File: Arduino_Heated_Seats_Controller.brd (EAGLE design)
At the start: 40.3 x 35.5 mm, 22 parts, among them U1 MEGA8-AI, U2 UA78M05CDCY, U3 ULN2003ADE4, U4 IC_TD62783-SO-18W

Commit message: Additional silkscreen and trace width tweaks before sending to OSH Park (still v4).
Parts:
- moved R1 0.06 mm to (14.0, 28.6)
- moved R2 0.06 mm to (16.6, 28.6)
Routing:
- net D3: track 24.0 -> 41.4 mm

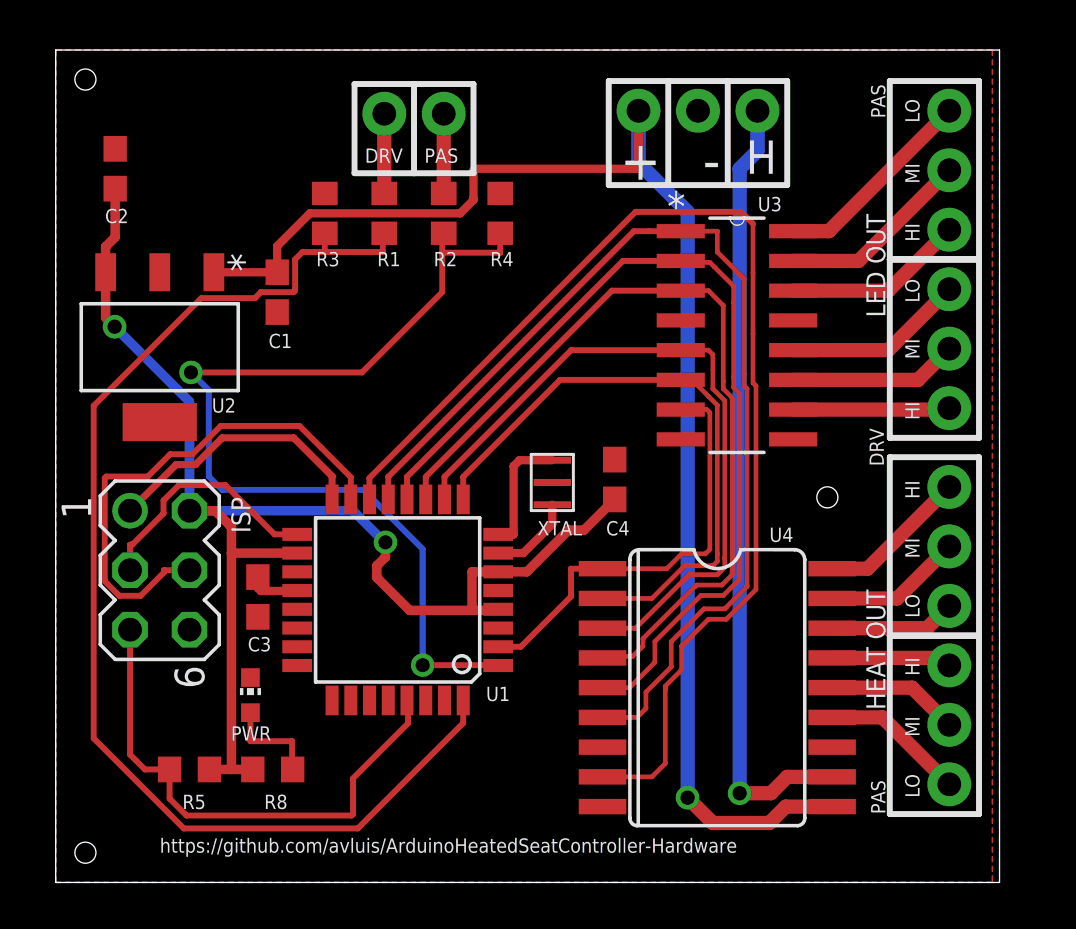
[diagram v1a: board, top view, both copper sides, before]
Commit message: Small position tweak to allow ground pour around connectors.
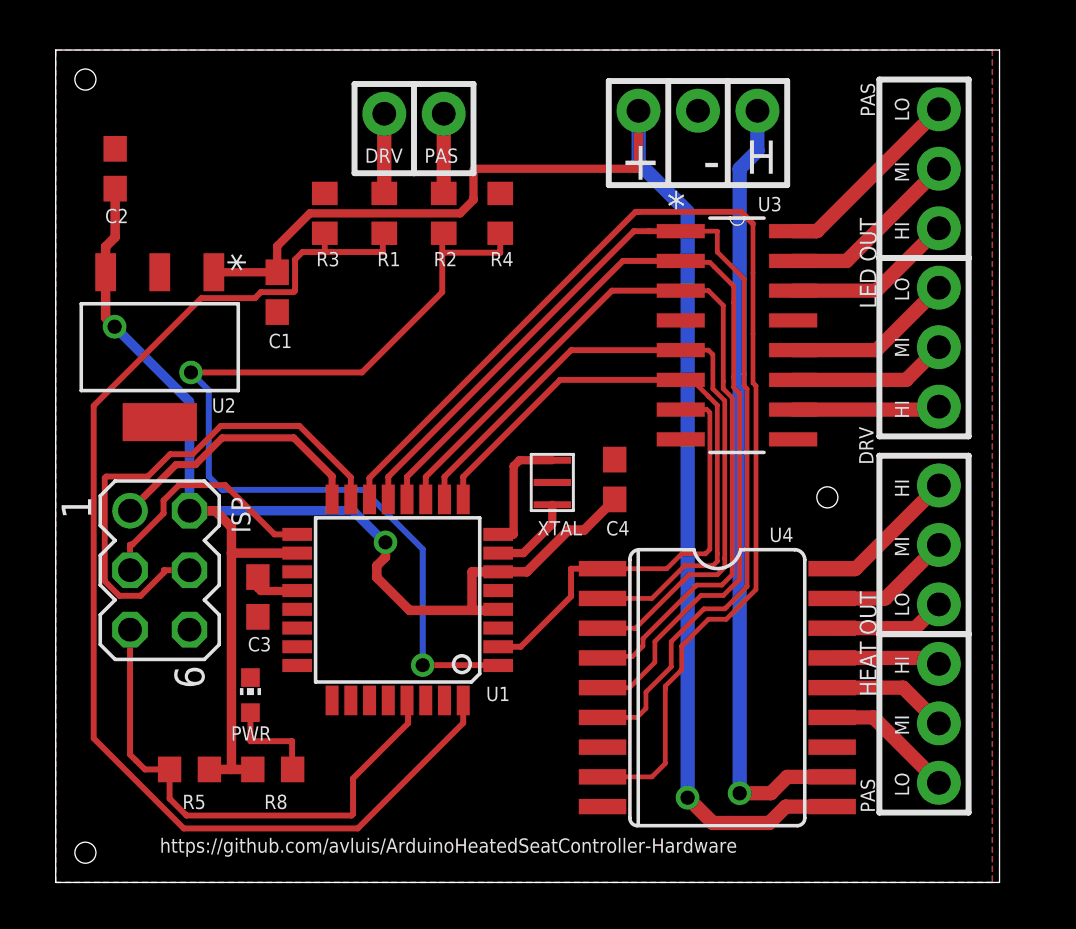
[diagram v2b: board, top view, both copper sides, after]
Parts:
- moved H-OUT 0.45 mm to (37.7, 17.0)
- moved LED-OUT 0.45 mm to (37.7, 20.3)

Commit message: Library error - need to make sure the rest of my libraries are correct are well.
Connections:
- net GND: now also U4.10; no longer U4.9
- net VIN: now also U4.9; no longer U4.10
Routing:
- net VIN: track 61.4 -> 58.5 mm
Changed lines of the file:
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@@
 <contactref element="PWR" pad="C"/>
 <contactref element="ISP" pad="6"/>
-<contactref element="U4" pad="9"/>
+<contactref element="U4" pad="10"/>
 <contactref element="U2" pad="4"/>
 <contactref element="U2" pad="2"/>
@@
 <signal name="VIN">
 <contactref element="PWR/H" pad="1"/>
-<contactref element="U4" pad="10"/>
+<contactref element="U4" pad="9"/>
 <contactref element="U2" pad="1"/>
 <contactref element="C1" pad="1"/>
 <wire x1="6.7564" y1="26.0604" x2="6.7564" y2="25.53575" width="0.254" layer="1"/>
-<wire x1="33.1597" y1="3.2385" x2="31.1785" y2="3.2385" width="0.6096" layer="1"/>
-<wire x1="31.1785" y1="3.2385" x2="30.48" y2="2.54" width="0.6096" layer="1"/>
-<wire x1="30.48" y1="2.54" x2="28.067" y2="2.54" width="0.6096" layer="1"/>
-<wire x1="28.067" y1="2.54" x2="26.9875" y2="3.6195" width="0.6096" layer="1"/>
 <via x="26.9875" y="3.6195" extent="1-16" drill="0.6096" diameter="1.016" shape="octagon"/>
 <wire x1="26.9875" y1="3.6195" x2="26.9875" y2="28.6385" width="0.6096" layer="16"/>
@@
 <wire x1="25.019" y1="30.607" x2="24.892" y2="30.734" width="0.6096" layer="16"/>
 <wire x1="24.892" y1="30.734" x2="24.892" y2="32.9565" width="0.6096" layer="16"/>
+<wire x1="26.9875" y1="3.6195" x2="26.9875" y2="3.2385" width="0.6096" layer="1"/>
+<wire x1="26.9875" y1="3.2385" x2="23.3553" y2="3.2385" width="0.6096" layer="1"/>
 </signal>
 <signal name="D4">

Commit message: More patching.
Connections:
- net VIN: now also U3.9
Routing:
- net VIN: track 58.5 -> 76.2 mm
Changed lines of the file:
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@@
 <wire x1="26.9875" y1="3.6195" x2="26.9875" y2="3.2385" width="0.6096" layer="1"/>
 <wire x1="26.9875" y1="3.2385" x2="23.3553" y2="3.2385" width="0.6096" layer="1"/>
+<contactref element="U3" pad="9"/>
+<wire x1="31.496" y1="18.923" x2="30.48" y2="17.907" width="0.4064" layer="1"/>
+<wire x1="30.48" y1="17.907" x2="30.48" y2="12.065" width="0.4064" layer="1"/>
+<wire x1="30.48" y1="12.065" x2="28.956" y2="10.541" width="0.4064" layer="1"/>
+<wire x1="28.956" y1="10.541" x2="28.0035" y2="10.541" width="0.4064" layer="1"/>
+<wire x1="28.0035" y1="10.541" x2="27.559" y2="10.0965" width="0.4064" layer="1"/>
+<wire x1="27.559" y1="10.0965" x2="27.559" y2="8.5725" width="0.4064" layer="1"/>
+<wire x1="27.559" y1="8.5725" x2="26.9875" y2="8.001" width="0.4064" layer="1"/>
+<wire x1="26.9875" y1="8.001" x2="26.9875" y2="3.6195" width="0.4064" layer="1"/>
 </signal>
 <signal name="D4">

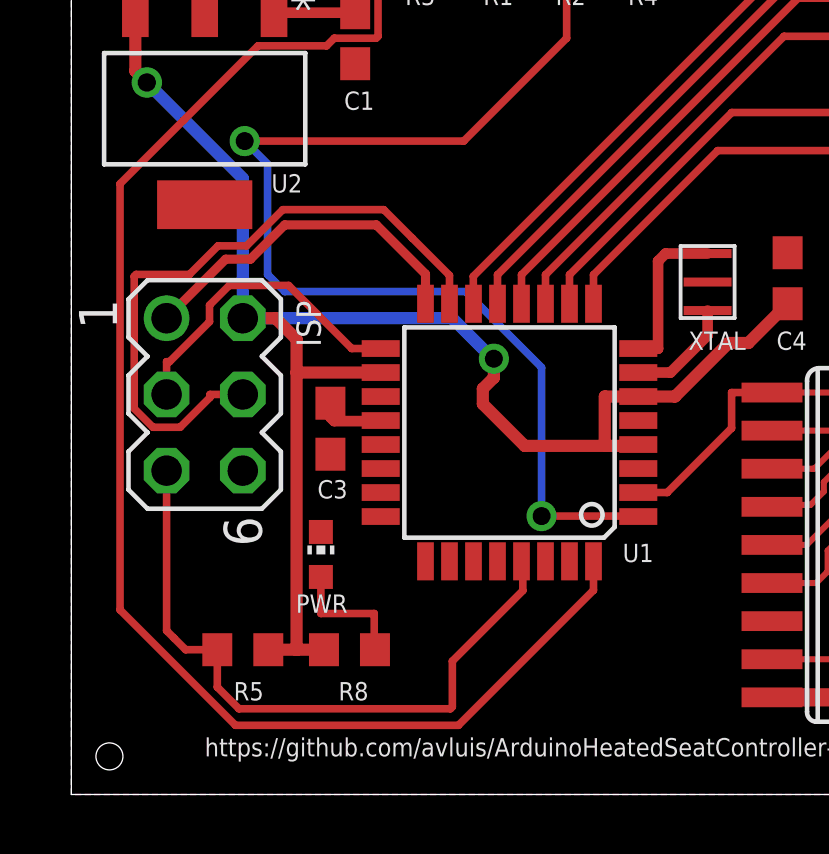
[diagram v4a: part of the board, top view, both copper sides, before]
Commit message: Grounding unused input pins (compatibility with A2982SLWTR-T). Tweak routing and vias.
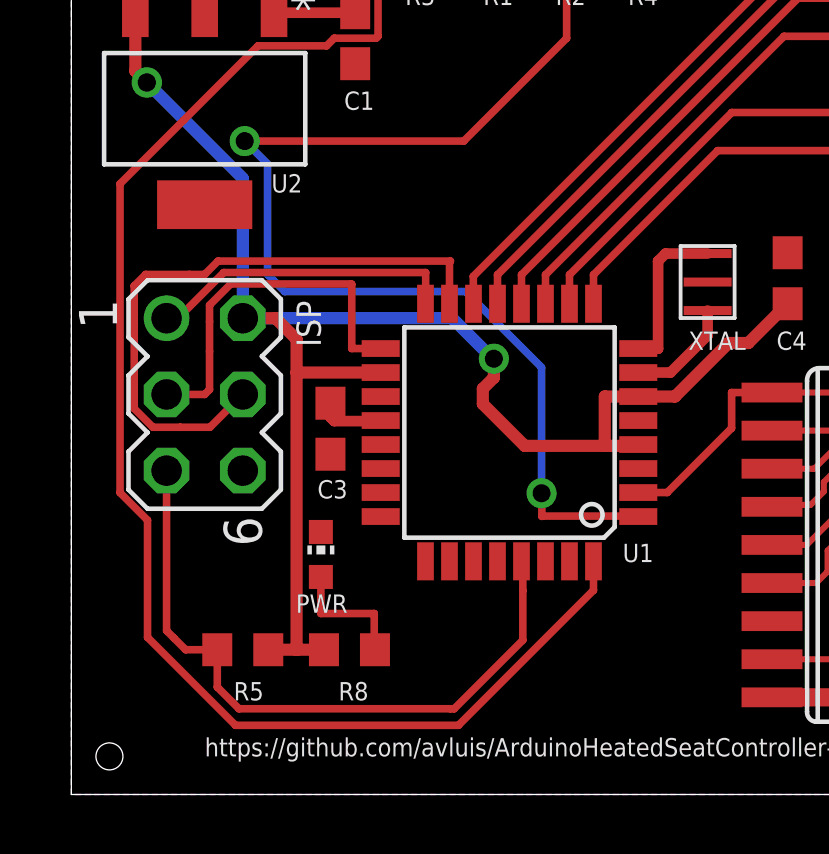
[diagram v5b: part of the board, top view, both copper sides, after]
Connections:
- net GND: now also U4.7
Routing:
- net D13: track 10.5 -> 12.5 mm
- net D11: track 22.1 -> 20.8 mm
- net D12: track 11.6 -> 10.3 mm

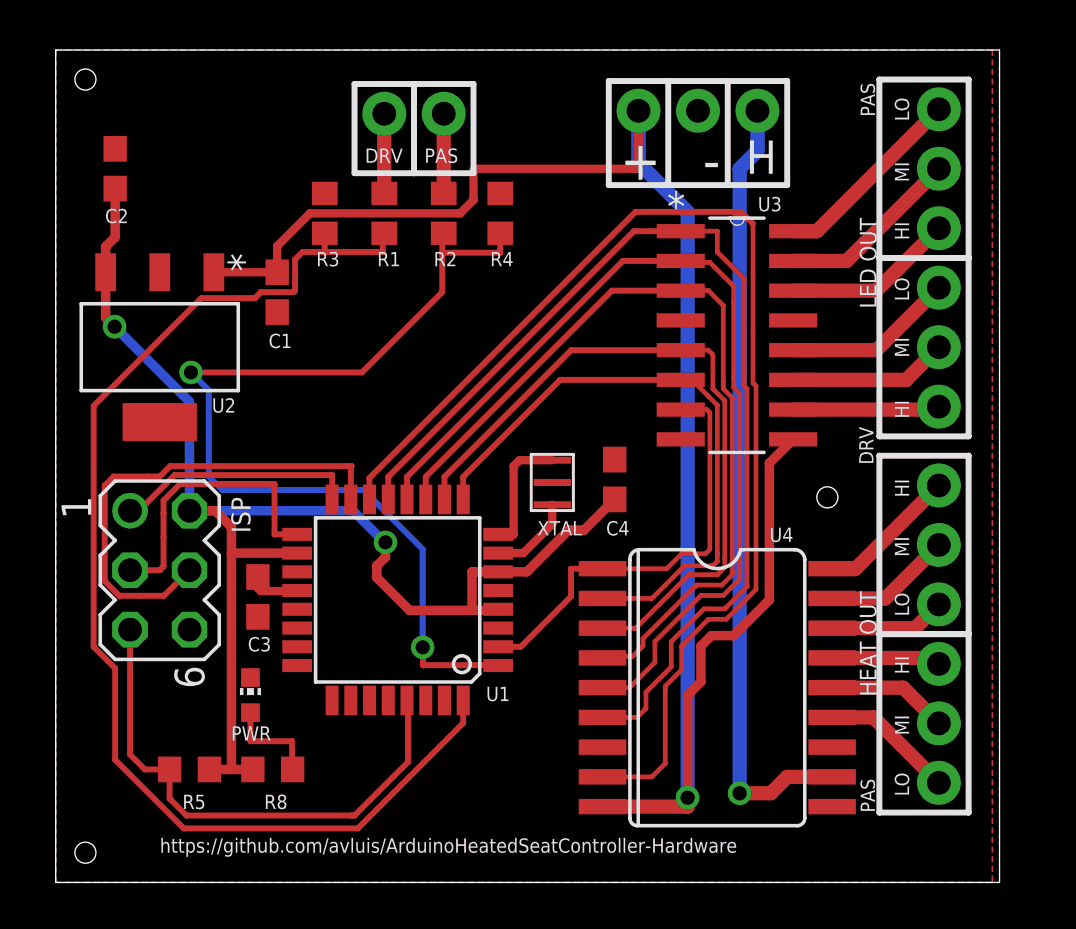
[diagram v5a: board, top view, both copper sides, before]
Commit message: Swapped ATMega from unknown library with Element14 library. Moved silkscreen (web address) to other side of board.
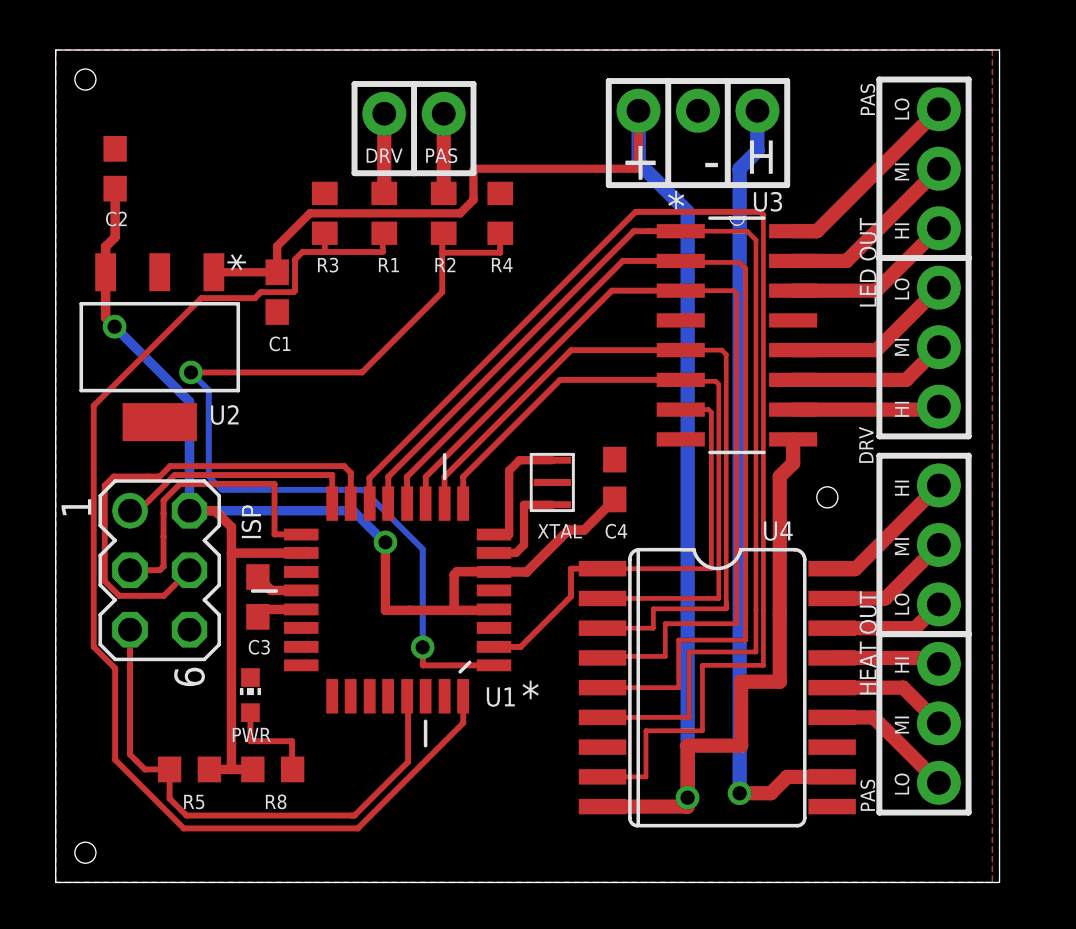
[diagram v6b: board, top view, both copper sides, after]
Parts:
- U1: value MEGA8-AI -> ATMEGA328P-AU; device atmel:TQFP32-08 -> Atmel_By_element14_Batch_1-00:QFP80P900X900X120-32N
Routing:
- net D9: track 44.6 -> 48.3 mm
- net D8: track 40.1 -> 43.6 mm
- net D10: track 50.3 -> 53.6 mm
- net D7: track 36.1 -> 39.0 mm
- net D6: track 30.3 -> 32.7 mm
- net GND: track 0.00 -> 1.99 mm
- net D5: track 26.2 -> 28.0 mm
- net VIN: track 76.2 -> 78.0 mm
- net VDD: track 57.9 -> 59.1 mm
- net D4: track 18.6 -> 19.4 mm
- net PB6: track 3.65 -> 4.35 mm

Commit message: Enough changes to warrant a minor revision bump. Equivalent parts have been selected for testing - will need to update design if tests are good. Current design should be compatible with selected parts (will order parts before sending to fab house).
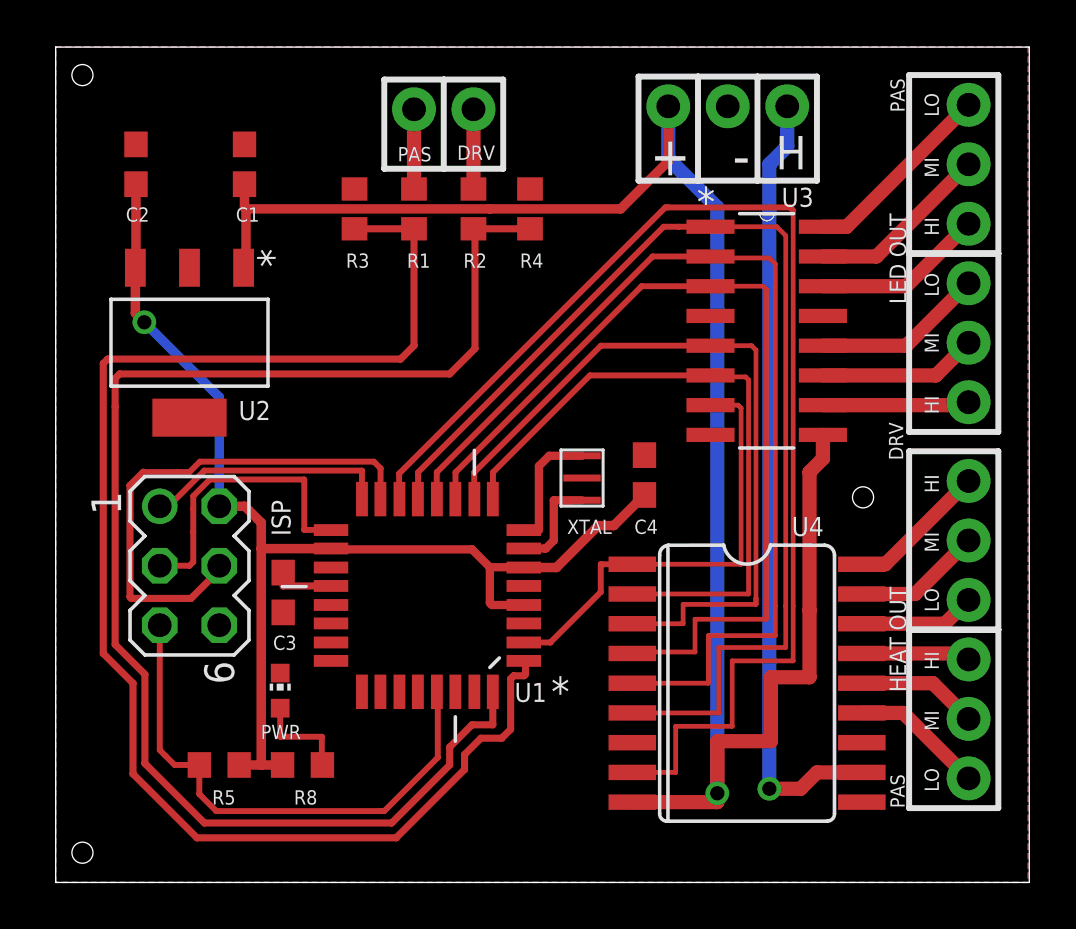
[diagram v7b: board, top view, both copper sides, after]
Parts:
- moved C1 5.64 mm to (8.06, 30.7), turned to 90 degrees
- moved R3 1.28 mm to (12.8, 28.8)
- moved R5 1.28 mm to (6.99, 5.02)
- moved BTN-IN 1.28 mm to (15.3, 33.0)
- moved C4 1.28 mm to (25.1, 17.4)
- moved PWR 1.28 mm to (9.59, 8.19)
- moved PWR/H 1.28 mm to (26.2, 33.1)
- moved R1 1.28 mm to (15.3, 28.8)
- moved R2 1.28 mm to (17.8, 28.8)
- moved R4 1.28 mm to (20.3, 28.8)
- moved R8 1.28 mm to (10.5, 5.02)
- moved U$1 1.28 mm to (29.4, 11.7)
- moved U1 1.28 mm to (15.9, 12.3)
- moved U2 1.28 mm to (5.71, 23.1)
- moved U3 1.28 mm to (32.8, 19.1)
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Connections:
- net D-BTN: now also BTN-IN.2, R2.1; no longer BTN-IN.1, R1.1
- net D2: now also R2.2, R4.1; no longer R1.2, R3.1
- net D3: now also R1.2, R3.1; no longer R2.2, R4.1
- net P-BTN: now also BTN-IN.1, R1.1; no longer BTN-IN.2, R2.1
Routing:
- net D3: track 41.2 -> 62.2 mm, vias 2 -> 0
- net VDD: track 59.1 -> 50.6 mm, vias 2 -> 1
- net D2: track 52.1 -> 59.9 mm
- net GND: track 1.99 -> 0.00 mm
- net VIN: track 78.0 -> 79.1 mm
- net D11: track 20.7 -> 21.8 mm
- net AREF: track 2.09 -> 2.62 mm
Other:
- board size 40.3 x 35.5 mm -> 41.6 x 35.7 mm
- board text added: "Arduino Powered Heated Seat Controller rev. 4a"
- board text removed: "Arduino Powered Heated Seat Controller rev. 4"

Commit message: Changes from freelancer.com - lovely~
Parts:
- removed PWR: (no value), led:CHIP-LED0603
- removed R8: 1k, resistor:R0603
- added L, ON: (no value), led:CHIP-LED0603
- added R6, R7: 1K, resistor:R0603
- R1, R2: value 15k -> 15K
- R3, R4, R5: value 10k -> 10K
- U2: value UA78M05CDCY -> UA78M05; device Texas Instruments_By_element14_Batch_1:SOT230P700X180-4N -> Roylib Regulator:SOT223
- U3: value ULN2003ADE4 -> TPL7407L; device Texas Instruments_By_element14_Batch_1:SOIC127P600X175-16N -> Roylib Drivers:SOIC16N
- U4: value IC_TD62783-SO-18W -> A2982; device dp_devices:SO-18L -> Roylib Drivers:SOIC20W
- moved C1 22.1 mm to (14.0, 9.35)
- moved C2 20.4 mm to (14.0, 13.2), turned to 270 degrees
- moved R5 20.1 mm to (3.05, 24.7), turned to 0 degrees
- moved C3 16.4 mm to (10.5, 28.8), turned to 180 degrees
- moved C4 15.0 mm to (14.9, 28.4), turned to 0 degrees
- moved U2 12.1 mm to (6.91, 11.0), turned to 90 degrees
- moved ISP 10.3 mm to (9.82, 4.09), turned to 180 degrees
- moved U3 10.2 mm to (23.9, 24.1)
- moved U1 10.1 mm to (11.5, 21.4), turned to 90 degrees
- moved U$1 10.0 mm to (20.1, 15.3)
- moved R3 9.13 mm to (3.66, 28.0)
- moved R1 8.83 mm to (6.50, 28.0)
- moved BTN-IN 7.76 mm to (7.58, 32.2)
- moved U4 7.56 mm to (22.1, 7.52), turned to 0 degrees
- moved H-OUT 6.81 mm to (32.5, 15.1)
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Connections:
- new net N$1: L.A, R6.2
- net D13: now also R6.1
- net DH-HIGH: now also U4.20; no longer U4.18
- net DH-LOW: now also U4.18; no longer U4.16
- net DH-MID: now also U4.19; no longer U4.17
- net GND: now also L.C, ON.C, U4.12; no longer PWR.C, U2.4, U4.10
- net H-ON: now also U4.13; no longer U4.11
- net N$3: now also ON.A, R7.2; no longer PWR.A, R8.2
- net PH-HIGH: now also U4.17; no longer U4.15
- net PH-LOW: now also U4.15; no longer U4.13
- net PH-MID: now also U4.16; no longer U4.14
- net VDD: now also R7.1; no longer R8.1
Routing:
- net D13: track 12.6 -> 70.1 mm, vias 0 -> 2
- net D3: track 62.2 -> 23.2 mm, vias 0 -> 2
- net D2: track 59.9 -> 22.1 mm, vias 0 -> 2
- net VDD: track 50.6 -> 85.5 mm, vias 1 -> 3
- net D12: track 10.5 -> 37.1 mm, vias 0 -> 1
- net D10: track 53.6 -> 27.8 mm, vias 0 -> 2
- net VIN: track 79.1 -> 54.5 mm, vias 1 -> 2
- net D11: track 21.8 -> 39.1 mm, vias 0 -> 1
- net D4: track 19.4 -> 28.8 mm, vias 0 -> 2
- net RESET: track 22.8 -> 29.8 mm, vias 0 -> 1
- net H-ON: track 33.7 -> 38.2 mm
- net D8: track 43.6 -> 39.6 mm
- net PH-LOW: track 5.72 -> 9.20 mm
- net D7: track 39.0 -> 35.6 mm
- net D6: track 32.7 -> 29.4 mm
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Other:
- board size 41.6 x 35.7 mm -> 35 x 35 mm
- board text added: "Arduino Powered Heated Seat Controller Rev. 4b"
- board text added: "https://goo.gl/t2CsID"
- board text removed: "Arduino Powered Heated Seat Controller rev. 4a"
- board text removed: "https://github.com/avluis/ArduinoHeatedSeatController-Hardware"
